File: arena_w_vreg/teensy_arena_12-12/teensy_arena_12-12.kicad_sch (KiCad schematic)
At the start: 6 parts, among them J2 Conn_01x04_Pin, J3 Conn_01x04_Pin

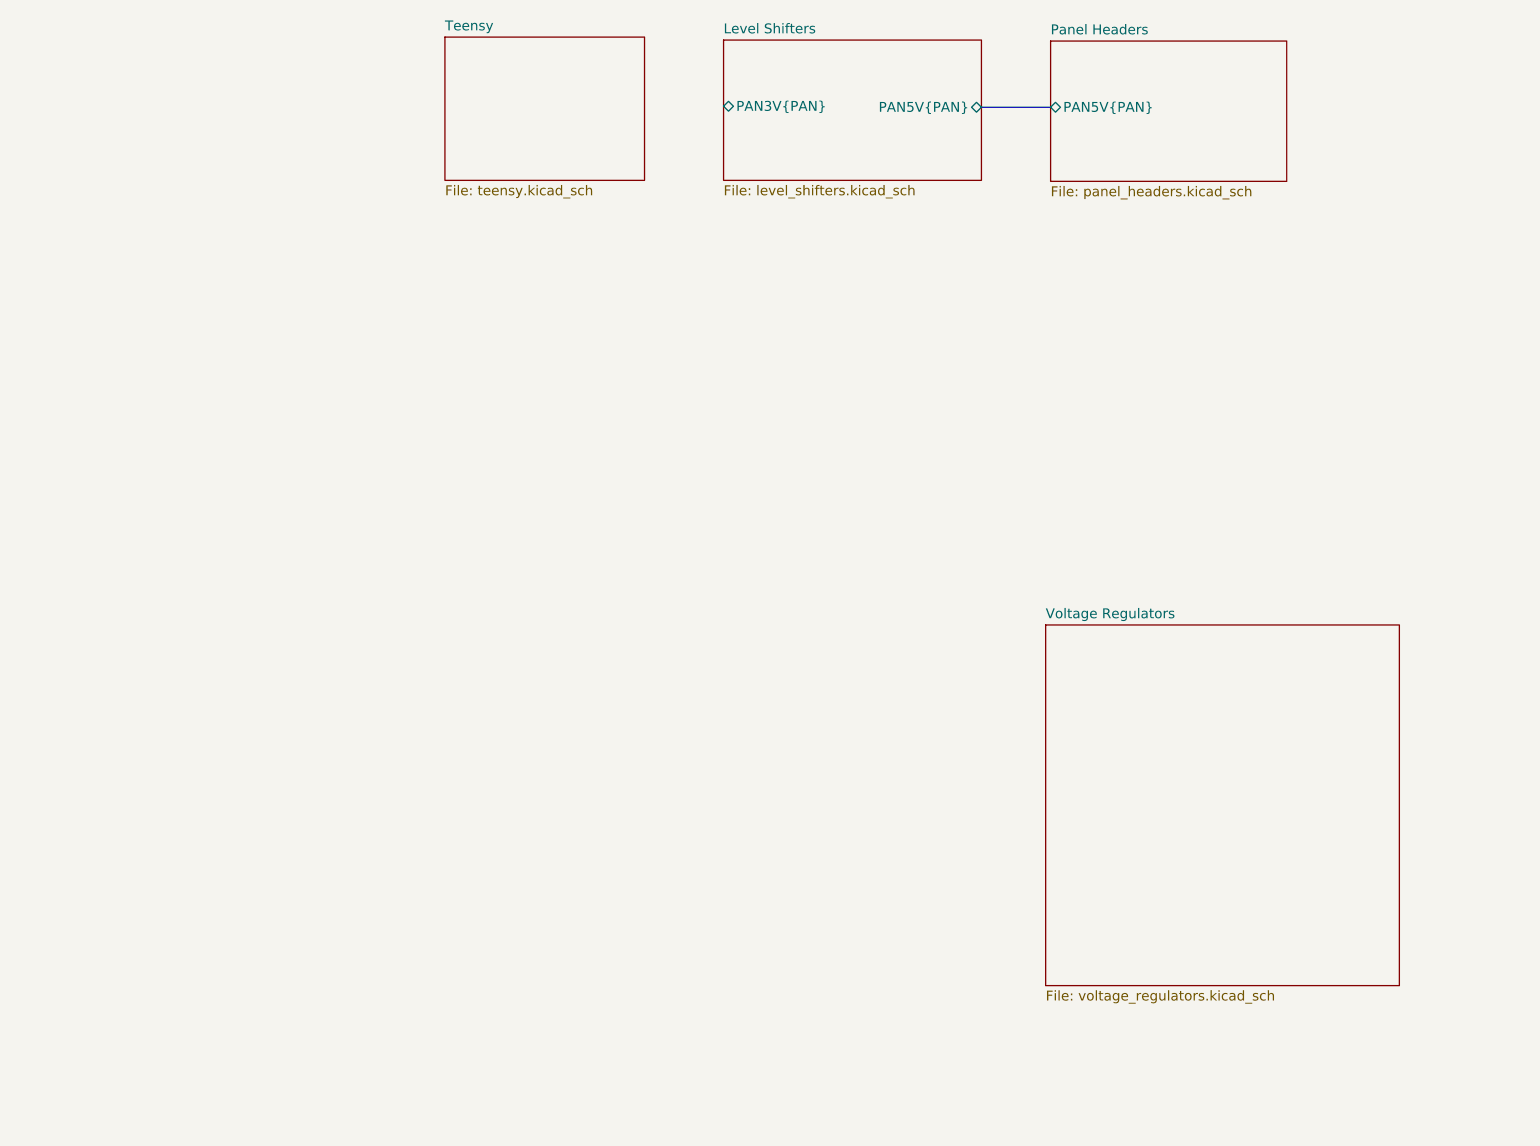
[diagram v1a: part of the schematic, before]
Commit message: Worked on 12-12 teensy arean with voltage regulators.
Moved MOSFET to panel headers sheet. Added RESET to level sifters. Added
decouple caps for TXB0108's.
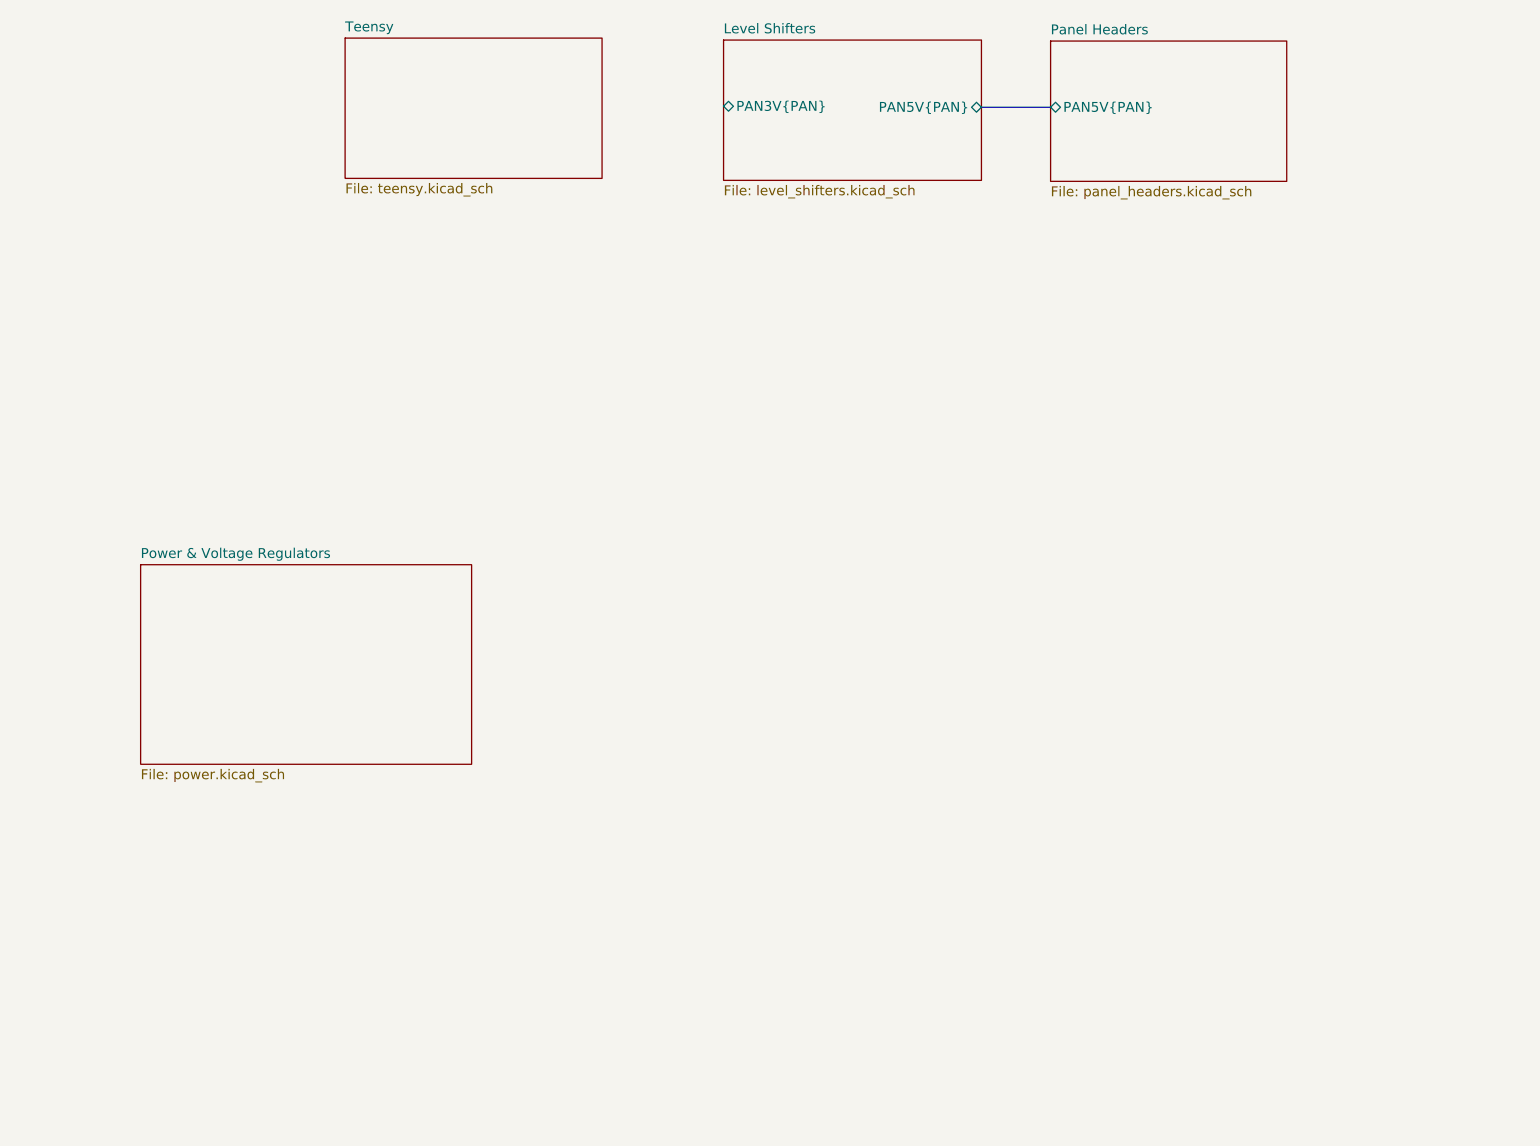
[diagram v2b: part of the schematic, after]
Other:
- removed sheet Voltage Regulators
- added sheet Power & Voltage Regulators (power.kicad_sch)
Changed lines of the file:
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@@
-    )
-  )
-  (sheet (at 165.608 108.077) (size 45.466 46.355) (fields_autoplaced)
-    (stroke (width 0.1524) (type solid))
-    (fill (color 0 0 0 0.0000))
-    (property "Sheetname" "Voltage Regulators" (at 165.608 107.3654 0)
-      (effects (font (size 1.27 1.27)) (justify left bottom))
-    )
-    (property "Sheetfile" "voltage_regulators.kicad_sch" (at 165.608 155.0166 0)
-      (effects (font (size 1.27 1.27)) (justify left top))
-    )
-    (instances
-      (project "teensy_arena_12-12"
-        (path "/a2511654-3a17-43f1-8b9e-c45e375533dc" (page "4"))
-      )
     )
   )
@@
     )
   )
-  (sheet (at 88.392 32.512) (size 25.654 18.415) (fields_autoplaced)
+  (sheet (at 49.276 100.33) (size 42.545 25.654) (fields_autoplaced)
     (stroke (width 0.1524) (type solid))
     (fill (color 0 0 0 0.0000))
-    (property "Sheetname" "Teensy" (at 88.392 31.8004 0)
+    (property "Sheetname" "Power & Voltage Regulators" (at 49.276 99.6184 0)
       (effects (font (size 1.27 1.27)) (justify left bottom))
     )
-    (property "Sheetfile" "teensy.kicad_sch" (at 88.392 51.5116 0)
+    (property "Sheetfile" "power.kicad_sch" (at 49.276 126.5686 0)
       (effects (font (size 1.27 1.27)) (justify left top))
     )
+    (instances
+      (project "teensy_arena_12-12"
+        (path "/a2511654-3a17-43f1-8b9e-c45e375533dc" (page "6"))
+      )
+    )
+  )
+  (sheet (at 75.565 32.639) (size 33.02 18.034) (fields_autoplaced)
+    (stroke (width 0.1524) (type solid))
+    (fill (color 0 0 0 0.0000))
+    (property "Sheetname" "Teensy" (at 75.565 31.9274 0)
+      (effects (font (size 1.27 1.27)) (justify left bottom))
+    )
+    (property "Sheetfile" "teensy.kicad_sch" (at 75.565 51.2576 0)
+      (effects (font (size 1.27 1.27)) (justify left top))
+    )

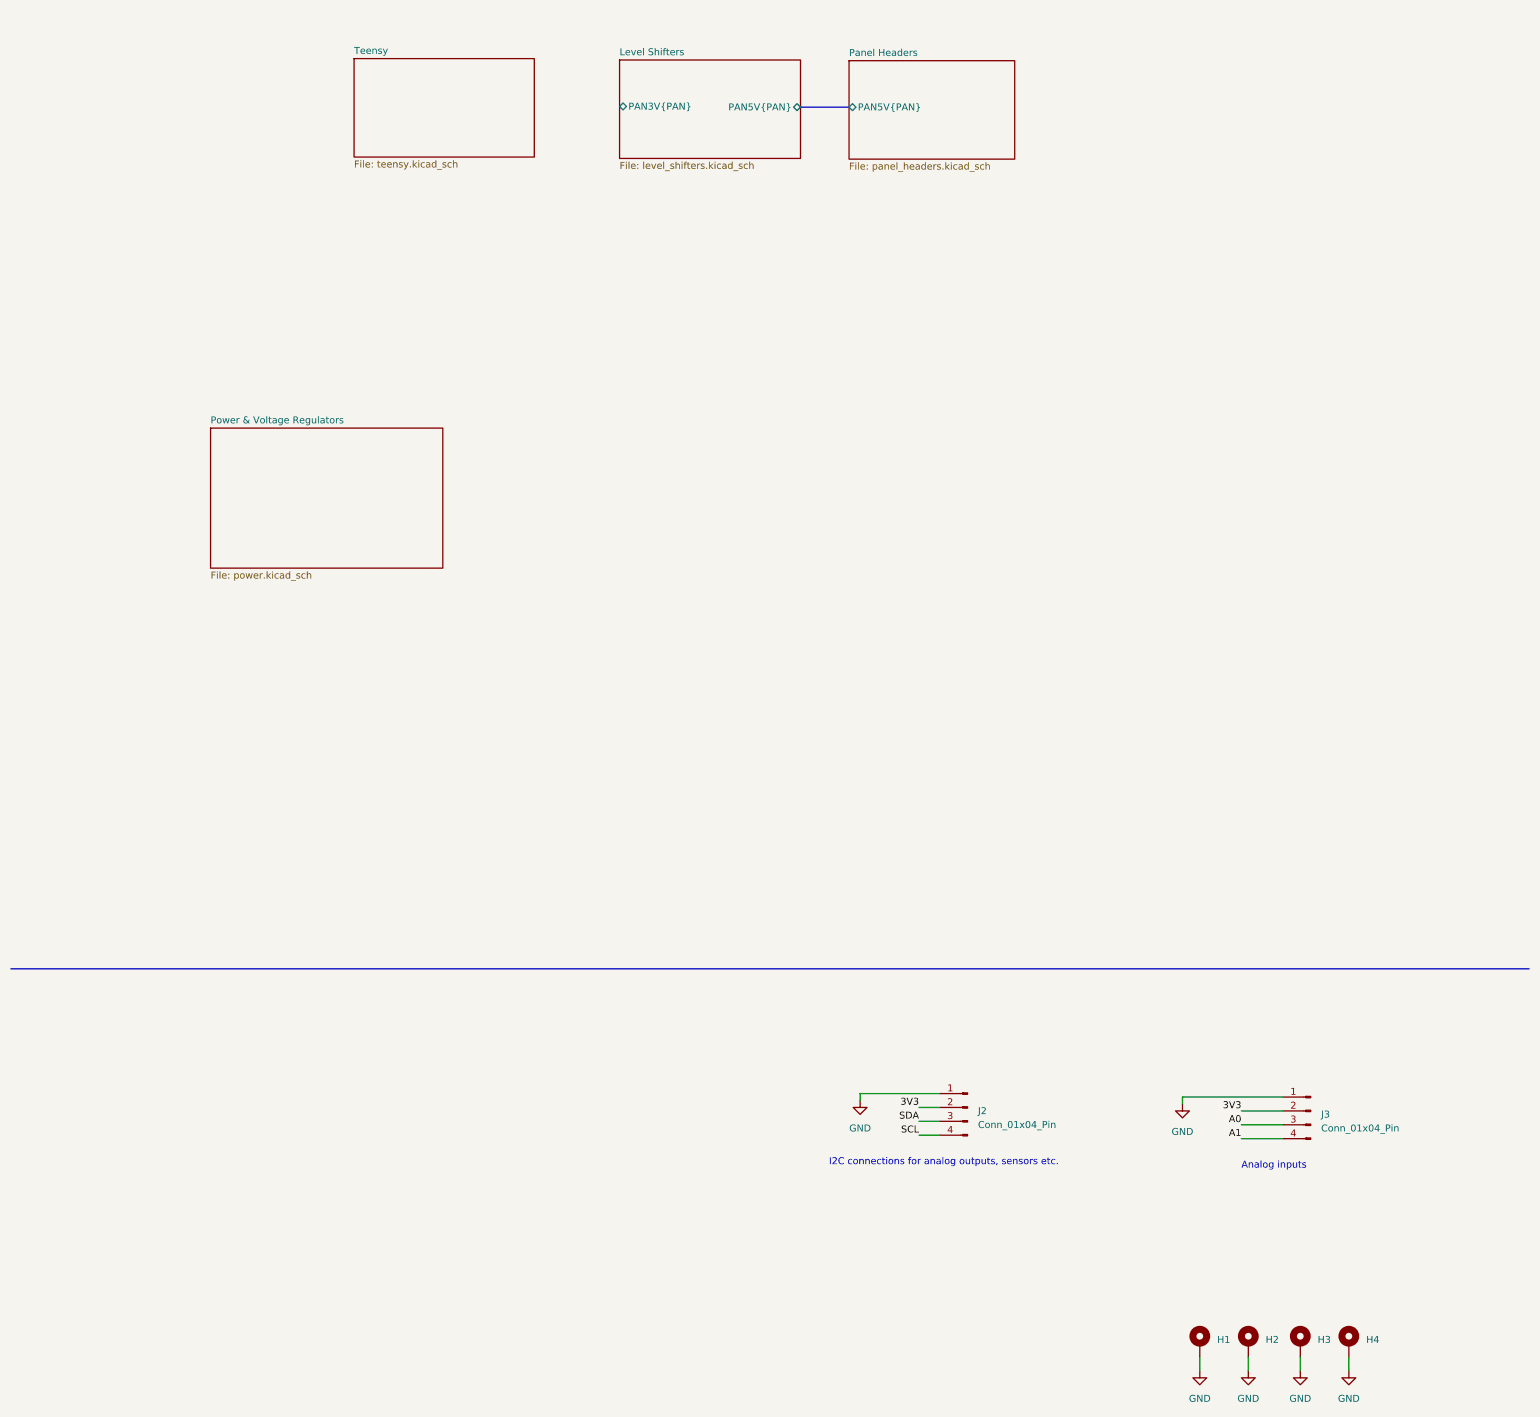
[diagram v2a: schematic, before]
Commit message: Completed initial schematic for 12-12 teensy arena.
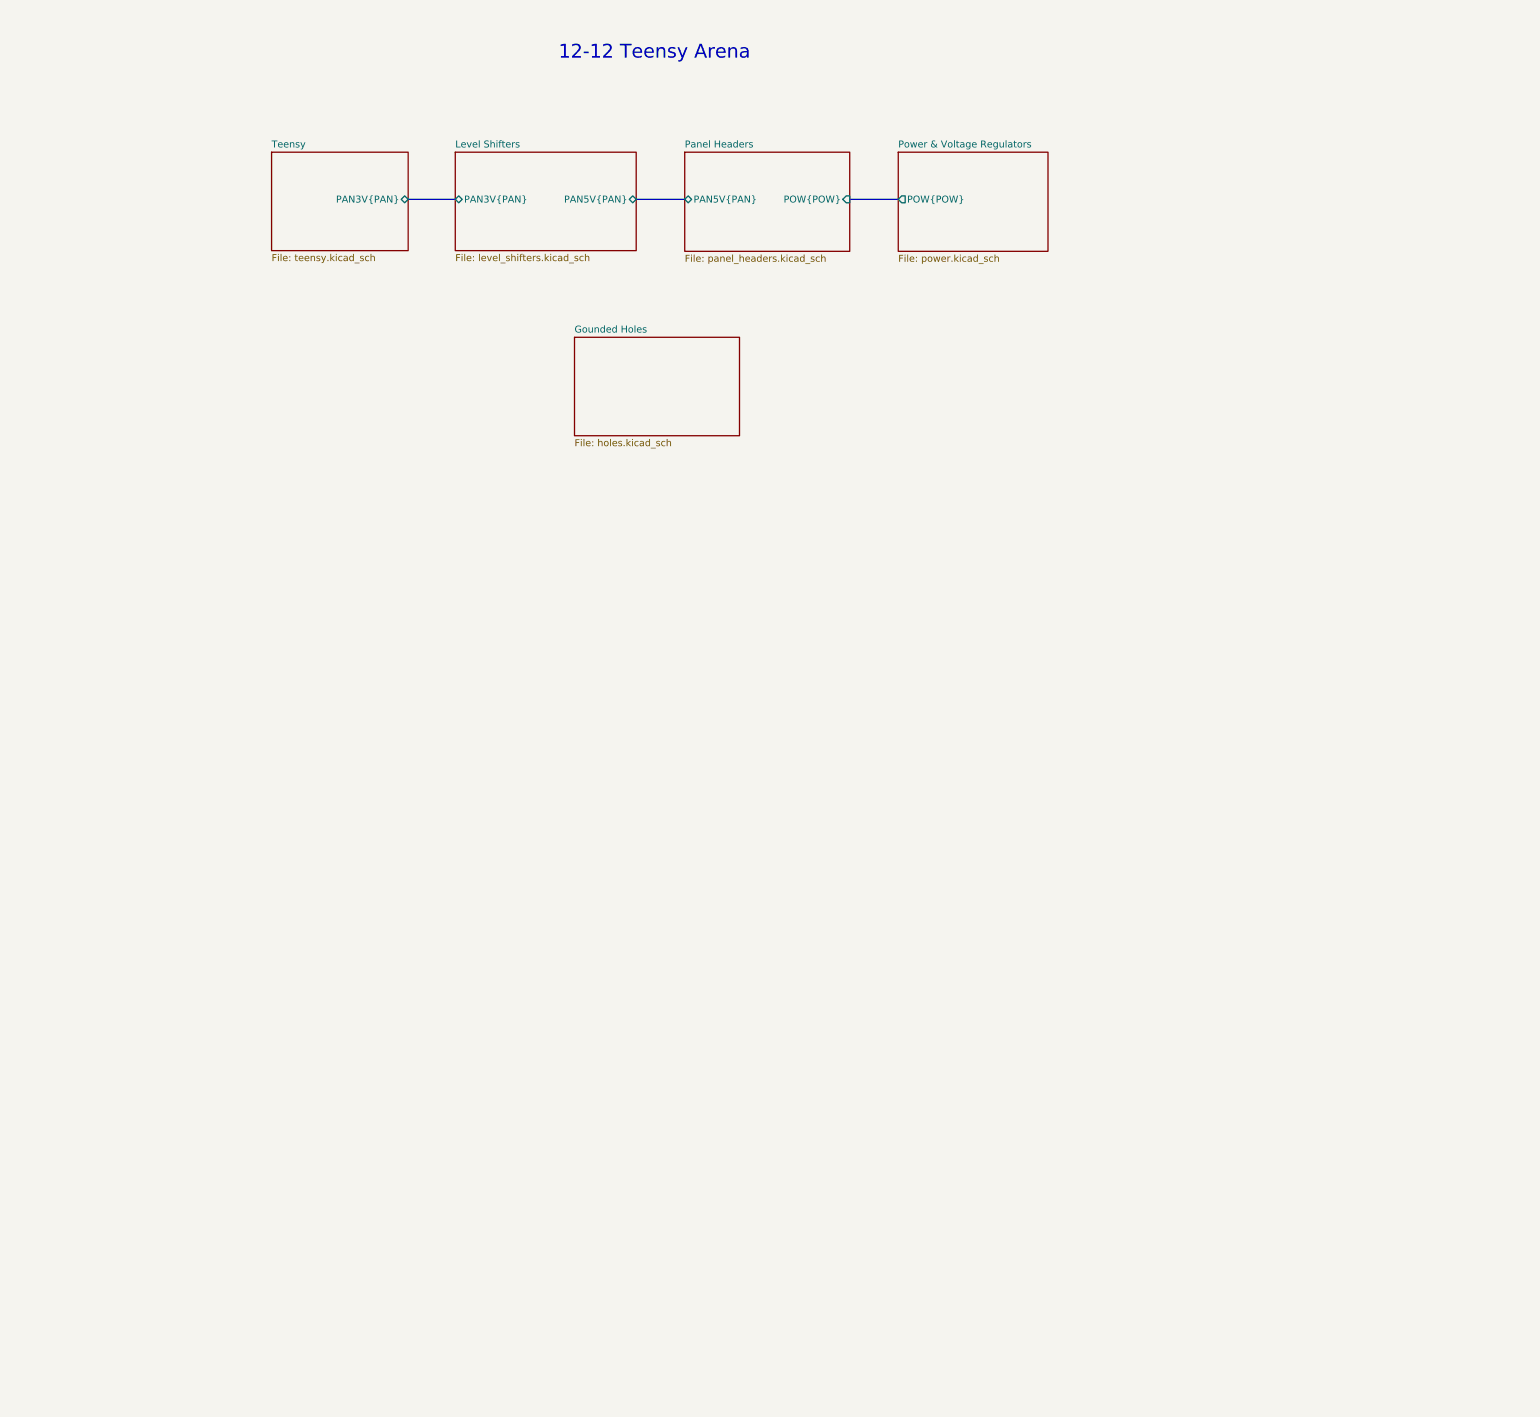
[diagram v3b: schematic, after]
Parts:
- removed H1, H2, H3, H4: MountingHole_Pad, MountingHole:MountingHole_3.2mm_M3_DIN965_Pad, symbol Mechanical:MountingHole_Pad
- removed J2, J3: Conn_01x04_Pin, arena_custom:NS-Tech_Grove_1x04_P2mm_Horizontal, symbol Connector:Conn_01x04_Pin
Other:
- added sheet Gounded Holes (holes.kicad_sch)
- sheet Panel Headers ports: added POW{POW}; removed none
- sheet Power & Voltage Regulators ports: added POW{POW}; removed none
- sheet Teensy ports: added PAN3V{PAN}; removed none
- note added: "12-12 Teensy Arena"
- note removed: "Analog inputs"
- note removed: "I2C connections for analog outputs, sensors etc."

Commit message: Wored on teensy arena.
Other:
- sheet Gounded Holes renamed Ground Holes
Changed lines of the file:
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@@
     (stroke (width 0.1524) (type solid))
     (fill (color 0 0 0 0.0000))
-    (property "Sheetname" "Gounded Holes" (at 115.951 82.9814 0)
+    (property "Sheetname" "Ground Holes" (at 115.951 82.9814 0)
       (effects (font (size 1.27 1.27)) (justify left bottom))
     )
